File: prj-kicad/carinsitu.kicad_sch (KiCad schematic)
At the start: 71 parts, among them P1 BAT, P2 MOT, P3 CONN_3, P4 CONN_4, SW1 SWITCH_SLIDE, SW2 Reset, U1 LoLin_D1_mini_pro, U2 MIC2860, U3 MAX17044G, U4 SN74LV1T34DBV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

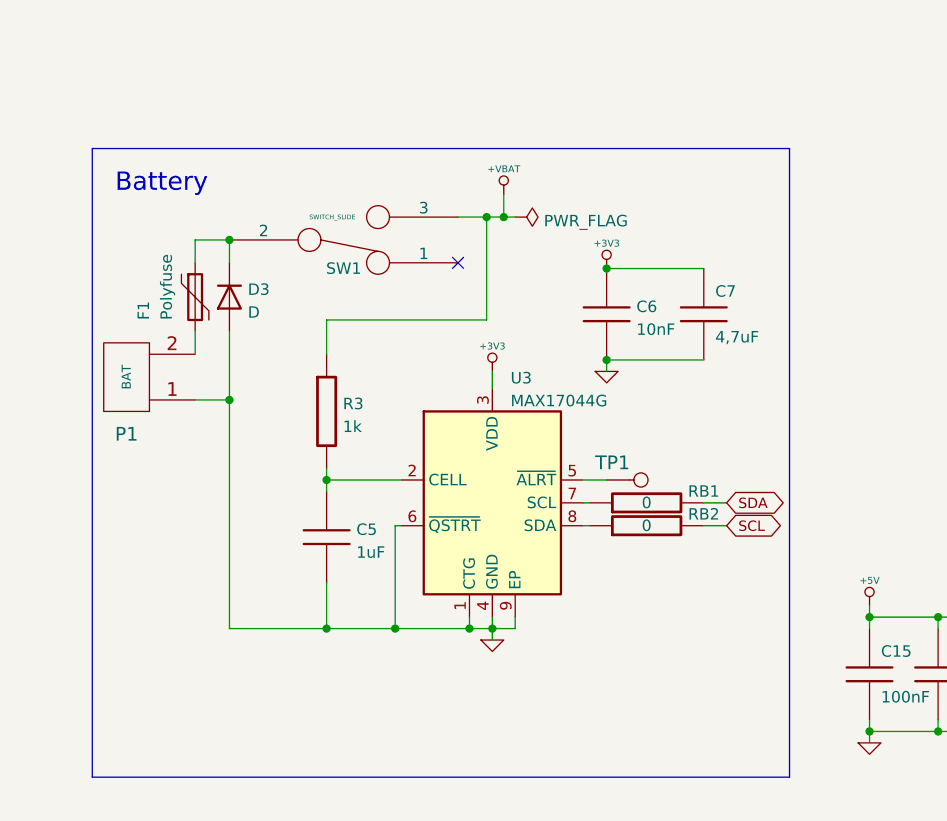
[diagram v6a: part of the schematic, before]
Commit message: Change input protection and its routing
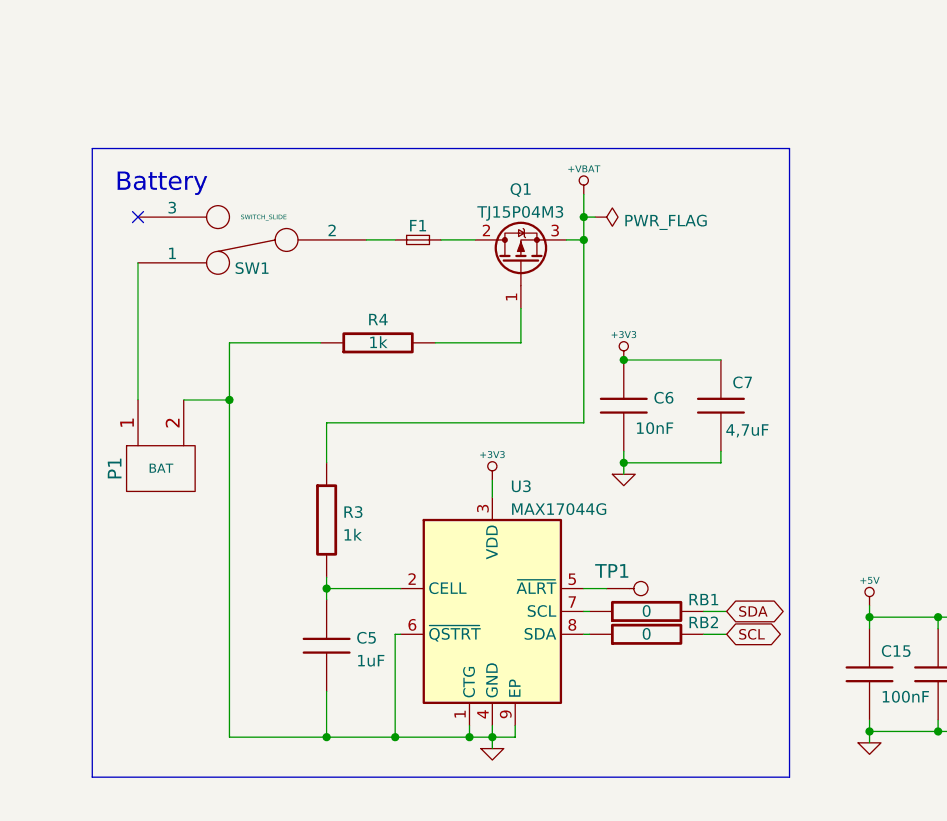
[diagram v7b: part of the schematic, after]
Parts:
- removed D3: D, Diode_THT:D_A-405_P2.54mm_Vertical_KathodeUp, symbol Device:D
- removed F1: Polyfuse, Fuse:Fuse_Bourns_MF-RG500, symbol Device:Polyfuse
- added F1: Fuse_Small, Fuse:Fuse_Littelfuse-LVR100, symbol Device:Fuse_Small
- added Q1: TJ15P04M3, Package_TO_SOT_SMD:TO-252-2, symbol Device:Q_PMOS_GDS
- added R4: 1k, Resistor_SMD:R_0805_2012Metric, symbol carinsitu:R
- H1: footprint (none) -> carinsitu:VTX_avatar_halfholes
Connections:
- net +VBAT: now also Q1.3 (S); no longer SW1.3
- net GND: now also P1.2 (PM), R4.1; no longer P1.1 (P1)
- net at SW1.1: now also P1.1 (P1)
- net at SW1.2: now also F1.1
- new net: Q1.1 (G), R4.2
- new net: F1.2, Q1.2 (D)
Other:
- moved on the sheet: C5, C6, C7, P1, R3, RB1, RB2, SW1, TP1, U3

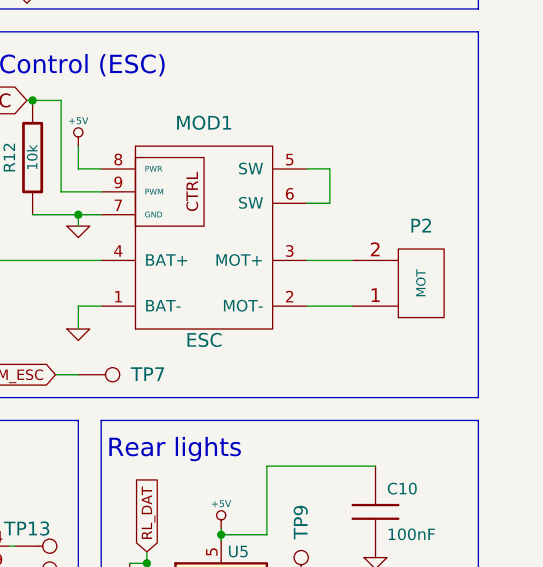
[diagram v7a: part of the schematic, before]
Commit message: Move Servo connector out of spacer + invert Motor connector to gain place
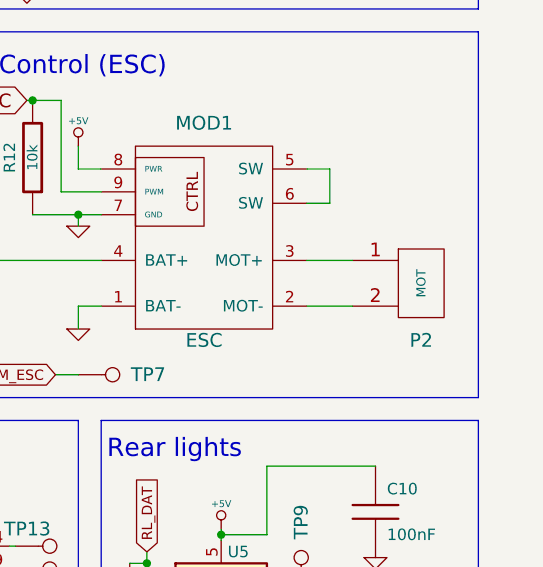
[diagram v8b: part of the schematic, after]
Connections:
- net at MOD1.2 (MOT-): now also P2.2 (PM); no longer P2.1 (P1)
- net at MOD1.3 (MOT+): now also P2.1 (P1); no longer P2.2 (PM)
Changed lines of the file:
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@@
     (pin "9")
   )
-  (symbol (lib_id "carinsitu:CONN_2") (at 275.59 62.23 0) (mirror x) (unit 1)
+  (symbol (lib_id "carinsitu:CONN_2") (at 275.59 62.23 0) (unit 1)
     (in_bom yes) (on_board yes)
-    (property "Reference" "P2" (id 0) (at 275.59 55.88 0)
+    (property "Reference" "P2" (id 0) (at 275.59 68.58 0)
       (effects (font (size 1.524 1.524)))
     )
